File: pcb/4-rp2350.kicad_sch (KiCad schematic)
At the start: 0 parts

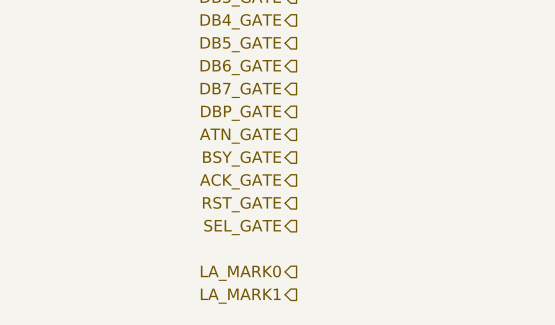
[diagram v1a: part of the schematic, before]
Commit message: Phase 3: populate SCSI sheet and channel sheets
SCSI sheet (A2): IDC50 and HD50 wired by signal name from SCSI-2
Table 2, all four RESERVED lines grounded through 0R links, the
logic-analyzer header as a pin-for-pin copy of the Digital Discovery
DIN connector, three SN74LVTH245A terminators with their DIP-switch
enable and truth table, and one cluster per line: 2 x 220R terminator
pair, ESD diode and channel sheet. Channel sheets hold the FDV301N
driver and the 74LVC1G17 receiver; 18 instances, references page x 100.

Generator: repeated sheets, sheet symbols, native tables, and
deterministic UUIDs. Nets renamed: LA -> LOGIC_ANALYZER,
TERMINATOR_EN -> TERMINATOR_EN_INVERTED_FIRMWARE.
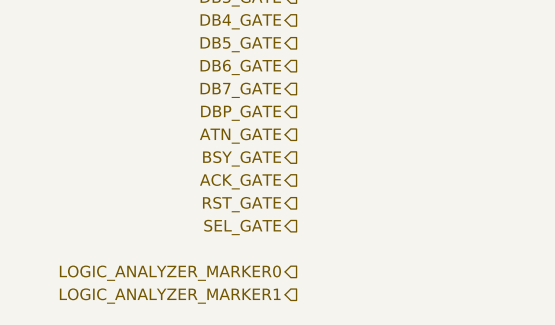
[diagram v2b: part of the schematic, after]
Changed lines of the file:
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@@
 		)
 	)
-	(hierarchical_label "LA_MARK0"
+	(hierarchical_label "LOGIC_ANALYZER_MARKER0"
 		(shape output)
 		(at 50.8 137.16 180)
@@
 		)
 	)
-	(hierarchical_label "LA_MARK1"
+	(hierarchical_label "LOGIC_ANALYZER_MARKER1"
 		(shape output)
 		(at 50.8 139.7 180)

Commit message: Phase 3: populate RP2350 sheet; FT_* nets renamed FT232H_*
RP2350 sheet (A2): RP2350B with every pin labelled by function and the
FT1248, marker and USB series resistors inline on their pins; core
regulator, per-pin decoupling (14 x 100 nF, count corrected), crystal,
QSPI flash and PSRAM in separate boxes, TC2030 debug pads and buttons,
the FT1248 rework links, and the TERMPWR sense divider on ADC6.

Generator: recursive derived-symbol flattening, small field fonts.
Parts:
- added C401, C402, C403, C404: 4.7uF 10V, Capacitor_SMD:C_0402_1005Metric, symbol Device:C
- added C405: 10uF 25V, Capacitor_SMD:C_0805_2012Metric, symbol Device:C
- added C406, C407, C408, C409, C410, C411, C412, C413, C414, C415, C416, C417, C418, C421, C422, C424: 100nF, Capacitor_SMD:C_0402_1005Metric, symbol Device:C
- added C419, C420: 15pF, Capacitor_SMD:C_0402_1005Metric, symbol Device:C
- added C423: 1uF 25V, Capacitor_SMD:C_0402_1005Metric, symbol Device:C
- added J401: TC2030-IDC, Connector:Tag-Connect_TC2030-IDC-FP_2x03_P1.27mm_Vertical, symbol Connector:TC2030
- added L401: 3.3uH, symbol Device:L
- added R401, R407, R408, R409, R410, R411, R412, R413: 33R, Resistor_SMD:R_0402_1005Metric, symbol Device:R
- added R402, R405, R406: 1k, Resistor_SMD:R_0402_1005Metric, symbol Device:R
- added R403: 3.3k, Resistor_SMD:R_0402_1005Metric, symbol Device:R
- added R404: 10k, Resistor_SMD:R_0402_1005Metric, symbol Device:R
- added R414, R415: 100R, Resistor_SMD:R_0402_1005Metric, symbol Device:R
- added R416, R417: 27R, Resistor_SMD:R_0603_1608Metric, symbol Device:R
- added R418, R419, R420, R421, R422, R423, R424, R425, R426, R427: 0R, Resistor_SMD:R_0402_1005Metric, symbol Device:R
- added R428, R429: 100k, Resistor_SMD:R_0402_1005Metric, symbol Device:R
- added SW401: BOOTSEL, symbol Switch:SW_Push
- added SW402: RUN, symbol Switch:SW_Push
- added U401: RP2350B, Package_DFN_QFN:QFN-80-1EP_10x10mm_P0.4mm_EP3.4x3.4mm, symbol MCU_RaspberryPi:RP2350B
- added U402: W25Q128JVSIQ, Package_SO:SOIC-8_5.3x5.3mm_P1.27mm, symbol Memory_Flash:W25Q128JVS
- added U403: APS6404L-3SQR-SN, Package_SO:SOIC-8_3.9x4.9mm_P1.27mm, symbol Memory_RAM:APS6404L-3SQRx-SN
- added Y401: 12MHz ABM8-272-T3, Crystal:Crystal_SMD_3225-4Pin_3.2x2.5mm, symbol Device:Crystal_GND24
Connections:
- net ACK_GATE: now also U401.37 (GPIO29)
- net ACK_RX: now also U401.9 (GPIO11)
- net ATN_GATE: now also U401.28 (GPIO27)
- net ATN_RX: now also U401.7 (GPIO9)
- net BSY_GATE: now also U401.36 (GPIO28)
- net BSY_RX: now also U401.8 (GPIO10)
- net CD_RX: now also U401.14 (GPIO15)
- net DB0_GATE: now also U401.18 (GPIO18)
- net DB0_RX: now also U401.77 (GPIO0)
- net DB1_GATE: now also U401.19 (GPIO19)
- net DB1_RX: now also U401.78 (GPIO1)
- net DB2_GATE: now also U401.20 (GPIO20)
- net DB2_RX: now also U401.79 (GPIO2)
- net DB3_GATE: now also U401.21 (GPIO21)
- net DB3_RX: now also U401.80 (GPIO3)
- net DB4_GATE: now also U401.22 (GPIO22)
- net DB4_RX: now also U401.1 (GPIO4)
- net DB5_GATE: now also U401.23 (GPIO23)
- net DB5_RX: now also U401.2 (GPIO5)
- net DB6_GATE: now also U401.25 (GPIO24)
- net DB6_RX: now also U401.3 (GPIO6)
- net DB7_GATE: now also U401.26 (GPIO25)
- net DB7_RX: now also U401.4 (GPIO7)
- net DBP_GATE: now also U401.27 (GPIO26)
- net DBP_RX: now also U401.6 (GPIO8)
- net I2C_SCL: now also R420.2
- net I2C_SDA: now also R418.2
- net IO_RX: now also U401.17 (GPIO17)
- net LOGIC_ANALYZER_MARKER0: now also R414.1
- net LOGIC_ANALYZER_MARKER1: now also R415.1
- net MSG_RX: now also U401.12 (GPIO13)
- net REQ_RX: now also U401.16 (GPIO16)
- net RST_GATE: now also U401.38 (GPIO30)
- net RST_RX: now also U401.11 (GPIO12)
- net SD_CLK: now also R422.2
- net SD_CMD: now also R424.2
- net SD_D0: now also R426.2
- net SEL_GATE: now also U401.39 (GPIO31)
- net SEL_RX: now also U401.13 (GPIO14)
- net USB_RP_D+: now also R416.1
- net USB_RP_D-: now also R417.1
- new net: R407.1, U401.40 (GPIO32)
- new net: R408.1, U401.42 (GPIO33)
- new net: R409.1, U401.43 (GPIO34)
- new net: R410.1, U401.44 (GPIO35)
- new net: R411.2, U401.52 (GPIO41/ADC1)
- new net: R412.2, U401.53 (GPIO42/ADC2)
- new net: R413.2, U401.54 (GPIO43/ADC3)
- new net: R414.2, U401.55 (GPIO44/ADC4)
- new net: R415.2, U401.56 (GPIO45/ADC5)
- new net: R417.2, U401.66 (USB_DM)
- new net: R416.2, U401.67 (USB_DP)
- new net: R405.2, SW401.1
- new net: C420.1, R402.1, Y401.3
- new net: R406.2, SW402.1
- new net +3V3: C402.1, C405.1, C406.1, C407.1, C408.1, C409.1, C410.1, C411.1, C412.1, C413.1, C417.1, C418.1, C421.1, C422.1, C423.1, J401.1, R401.1, R403.1, R404.1, U401.15 (IOVDD), U401.24 (IOVDD), U401.29 (IOVDD), U401.41 (IOVDD), U401.5 (IOVDD), U401.50 (IOVDD), U401.59 (ADC_AVDD), U401.60 (IOVDD), U401.64 (VREG_VIN), U401.68 (USB_OTP_VDD), U401.69 (QSPI_IOVDD), U401.76 (IOVDD), U402.8 (VCC), U403.8 (VDD)
- new net DVDD_1V1: C403.1, C404.1, C414.1, C415.1, C416.1, L401.2, U401.10 (DVDD), U401.32 (DVDD), U401.51 (DVDD), U401.65 (VREG_FB)
- new net FT232H_D4: R419.2
- new net FT232H_D5: R421.2
- new net FT232H_D6: R423.2
- new net FT232H_D7: R425.2
- new net FT232H_MIOSIO0: R407.2
- new net FT232H_MIOSIO1: R408.2
- new net FT232H_MIOSIO2: R409.2
- new net FT232H_MIOSIO3: R410.2
- new net FT232H_MISO: R413.1
- new net FT232H_SCLK: R411.1
- new net FT232H_SS_N: R412.1
- new net FT232H_WR_N: R427.2
- new net GND: C401.2, C402.2, C403.2, C404.2, C405.2, C406.2, C407.2, C408.2, C409.2, C410.2, C411.2, C412.2, C413.2, C414.2, C415.2, C416.2, C417.2, C418.2, C419.2, C420.2, C421.2, C422.2, C423.2, C424.2, J401.5, R429.2, SW401.2, SW402.2, U401.62 (VREG_PGND), U401.81 (GND), U402.4 (GND), U403.4 (VSS), Y401.2 (G), Y401.4 (G)
- new net GPIO36: R418.1, R419.1, U401.45 (GPIO36)
- new net GPIO37: R420.1, R421.1, U401.46 (GPIO37)
- new net GPIO38: R422.1, R423.1, U401.47 (GPIO38)
- new net GPIO39: R424.1, R425.1, U401.48 (GPIO39)
- new net GPIO40: R426.1, R427.1, U401.49 (GPIO40/ADC0)
- new net PSRAM_CE_INVERTED: R403.2, U401.58 (GPIO47/ADC7), U403.1 (~{CE})
- new net QSPI_SCLK: U401.71 (QSPI_SCLK), U402.6 (CLK), U403.6 (SCLK)
- new net QSPI_SD0: U401.72 (QSPI_SD0), U402.5 (DI/IO_{0}), U403.5 (SI/SIO0)
- new net QSPI_SD1: U401.74 (QSPI_SD1), U402.2 (DO/IO_{1}), U403.2 (SO/SIO1)
- new net QSPI_SD2: U401.73 (QSPI_SD2), U402.3 (~{WP}/IO_{2}), U403.3 (SIO2)
- new net QSPI_SD3: U401.70 (QSPI_SD3), U402.7 (~{HOLD}/~{RESET}/IO_{3}), U403.7 (SIO3)
- new net QSPI_SS_INVERTED: R404.2, R405.1, U401.75 (~{QSPI_SS}), U402.1 (~{CS})
- new net RUN: J401.3, R406.1, U401.35 (RUN)
- new net SWCLK: J401.4, U401.33 (SWCLK)
- new net SWDIO: J401.2, U401.34 (SWDIO)
- new net TERMPWR: R428.1
- new net TERMPWR_SENSE: C424.1, R428.2, R429.1, U401.57 (GPIO46/ADC6)
- new net VREG_AVDD: C401.1, R401.2, U401.61 (VREG_AVDD)
- new net VREG_LX: L401.1, U401.63 (VREG_LX)
- new net XIN: C419.1, U401.30 (XIN), Y401.1
- new net XOUT: R402.2, U401.31 (XOUT)
- no-connect marks 0 -> 1
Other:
- note added: "0.5 x TERMPWR on GPIO 46: 0-5.6 V -> 0-2.8 V. Draws 26 uA from TERMPWR."
- note added: "ABM8-272-T3 (CL 10 pF, ESR <= 50 R): 2 x 15 pF (7.5 pF + ~3 pF stray), 1k series on XOUT stops overdrive."
- note added: "ADC_AVDD 59"
- note added: "APS6404L-3SQR-SN, 8 MB, on CS1 = GPIO 47: the stall buffer between SCSI and the host."
- note added: "BOOTSEL pulls QSPI_SS low through 1k at reset; RUN has no pull-up (the guide fits none; the RP2350 pulls RUN up internally)."
- note added: "C402 CIN, C403 COUT, C404 2nd DVDD (all 4.7 uF 0402; fallback 0603 C19666 for CIN if DC bias bites)."
- note added: "Core regulator (on-chip, 1.1 V)"
- note added: "Crystal (12 MHz)"
- note added: "DVDD 10"
- note added: "DVDD 32"
- note added: "DVDD 51"
- note added: "Debug and buttons"
- note added: "Decoupling (100 nF per supply pin, at the pin)"
- note added: "FT1248 rework links"
- note added: "Firmware keeps GPIO 46's digital input buffer off (analog use)."
- note added: "Fitted 0R: GPIO 36-40 -> I2C / microSD (normal). Unfitted 0R: the same GPIO -> FT232H pins 17-20, 27. Moving the links trades I2C + microSD for 8-bit FT1248 (36-39) or 245-FIFO mode (36-40)."
- note added: "Guide 2.1 / datasheet 6.3.8. Layout: inductor orientation per Fig. 23, VREG_PGND and CIN straight to the exposed pad, and a ground cut-out under VREG_LX on layer 2 (Fig. 24)."
- note added: "I2C0 SCL (rework: FT232H_D5)"
- note added: "I2C0 SDA (rework: FT232H_D4)"
- note added: "IOVDD 15"
- note added: "IOVDD 24"
- note added: "IOVDD 29"
- note added: "IOVDD 41"
- note added: "IOVDD 5"
- note added: "IOVDD 50"
- note added: "IOVDD 60"
- note added: "IOVDD 76"
- note added: "PSRAM"
- note added: "PWR_FLAGs: DVDD_1V1 is fed through L401 and VREG_AVDD through R401, which ERC sees as passive parts."
- note added: "Pin map: blocks/5-rp2350-pinout.md. GPIO 0-17 = receiver outputs (PIO0 in, read inverted), GPIO 18-31 = driver gates (1 = asserted). The only ground is the exposed pad (pin 81). Series resistors sit at the pins: 33R on the 7 FT1248 nets (damps ringing at 25 MHz, limits contention), 100R on the logic-analyzer markers, 27R 0603 on native USB (close to the chip)."
- note added: "Polarity dot per datasheet Fig. 23; check JLC's placement preview."
- note added: "QSPI flash"
- note added: "R403 3.3k: the RP2350 pulls GPIO 47 low at reset (36k min); 10k gave 2.58 V, under the PSRAM's VIH (VDD - 0.4 V). 3.3k gives 3.02 V."
- note added: "R404 DNP: this flash doesn't need a CS pull-up (guide R1)."
- note added: "RP2350B"
- note added: "TERMPWR sense (ADC6)"
- note added: "Tag-Connect TC2030-IDC pads (no part on the BOM) for the J-Link EDU via an ARM20-CTX adapter. BOOTSEL + reset = USB bootloader; normally the host enters BOOTSEL in software."
- note added: "Top pins: USB_OTP_VDD, ADC_AVDD, QSPI_IOVDD, IOVDD (x8) and VREG_VIN share +3V3; VREG_FB and DVDD (x3) are the 1.1 V core rail (DVDD_1V1), made by the on-chip regulator. Each supply pin gets its own 100 nF (Decoupling box)."
- note added: "USB_OTP 68+ QSPI 69"
- note added: "W25Q128JVSIQ, 16 MB, on the dedicated chip select (QSPI_SS). Boot + firmware."
- note added: "microSD CLK (rework: FT232H_D6)"
- note added: "microSD CMD (rework: FT232H_D7)"
- note added: "microSD D0 (rework: FT232H_WR_N)"
- note removed: "RP2350B and support (blocks/3-mcu-support.md, pin map blocks/5-rp2350-pinout.md) RP2350B + core regulator (3.3 µH, 4 × 4.7 µF, 33 Ω), decoupling, 12 MHz crystal, W25Q128 flash, APS6404L PSRAM (CS1 = GPIO 47, 3.3 k up), TC2030 SWD, BOOTSEL/RUN, 27 Ω USB series R, 33 Ω FT1248 series R, FT1248 rework 0 Ω links (GPIO 36-40), LA marker 100 Ω, TERMPWR ADC divider 100 k/100 k + 100 nF on GPIO 46."

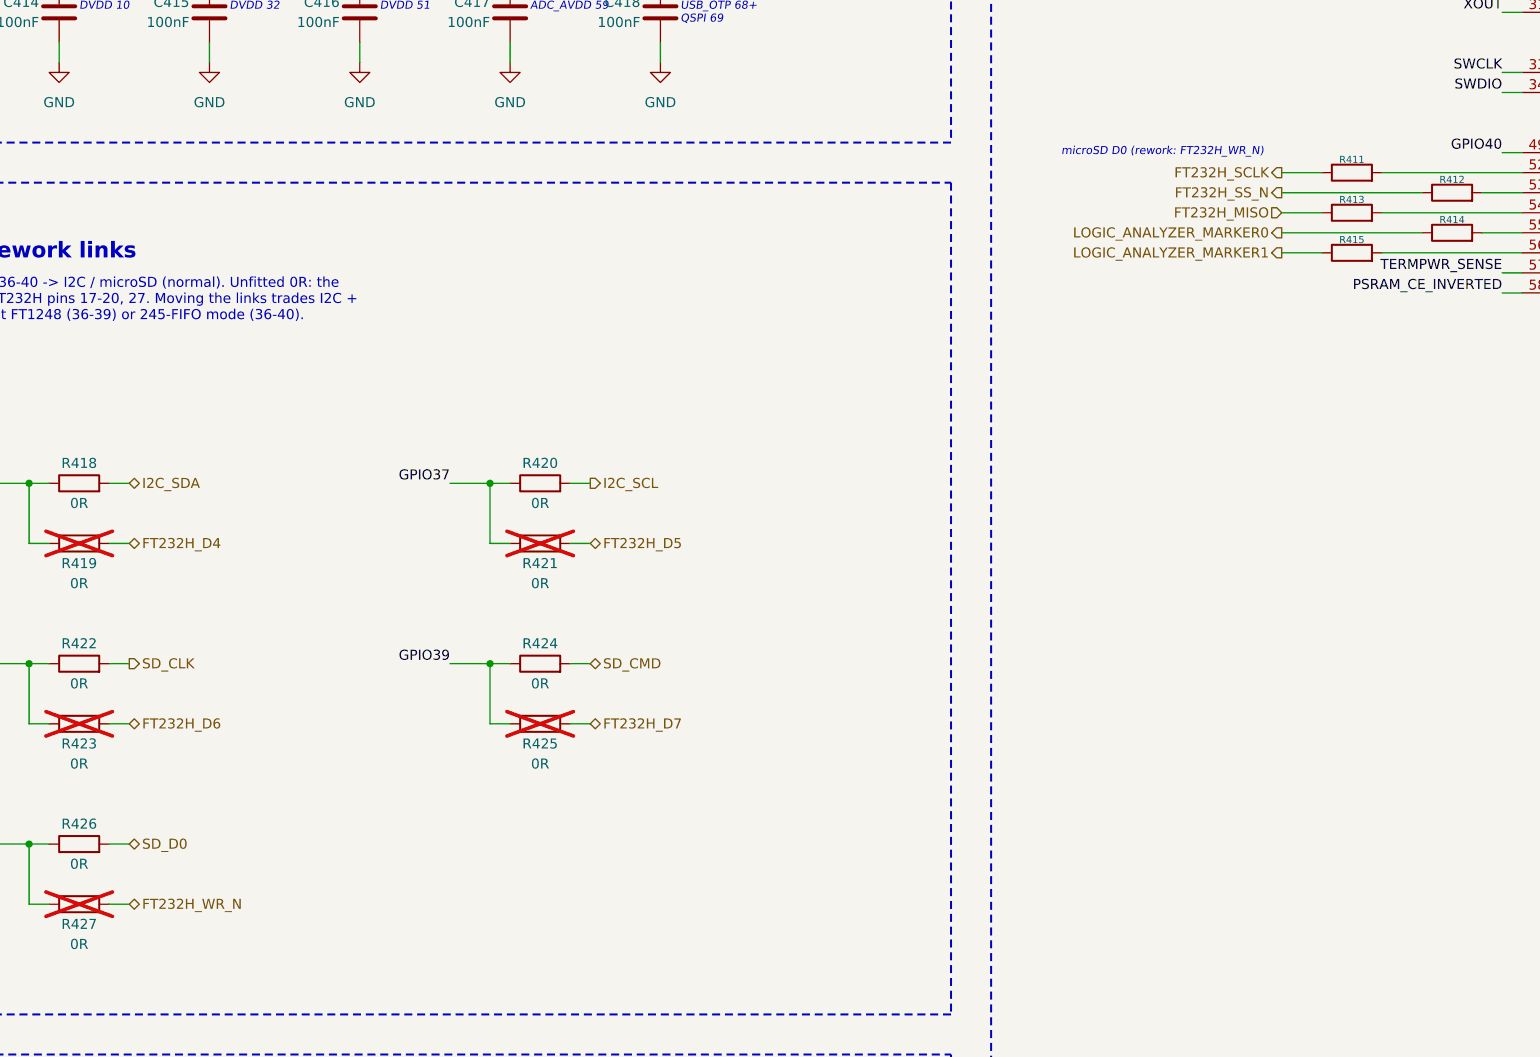
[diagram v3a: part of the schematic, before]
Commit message: Phase 3: populate FT232H sheet; FT232H_WR_N -> FT232H_WRITE_INVERTED
FT232HL per DS Fig. 6.2 (VCCD makes FT232H_3V3), ferrite-fed VPHY/VPLL,
93LC56B config EEPROM, crystal, REF, RESET RC and FIFO-fallback pull-ups.
Project FT232H symbol retypes EECS/EECLK as outputs (and VCCD as
power_out); upstream fix recorded as a follow-up (NOTES open question 14).
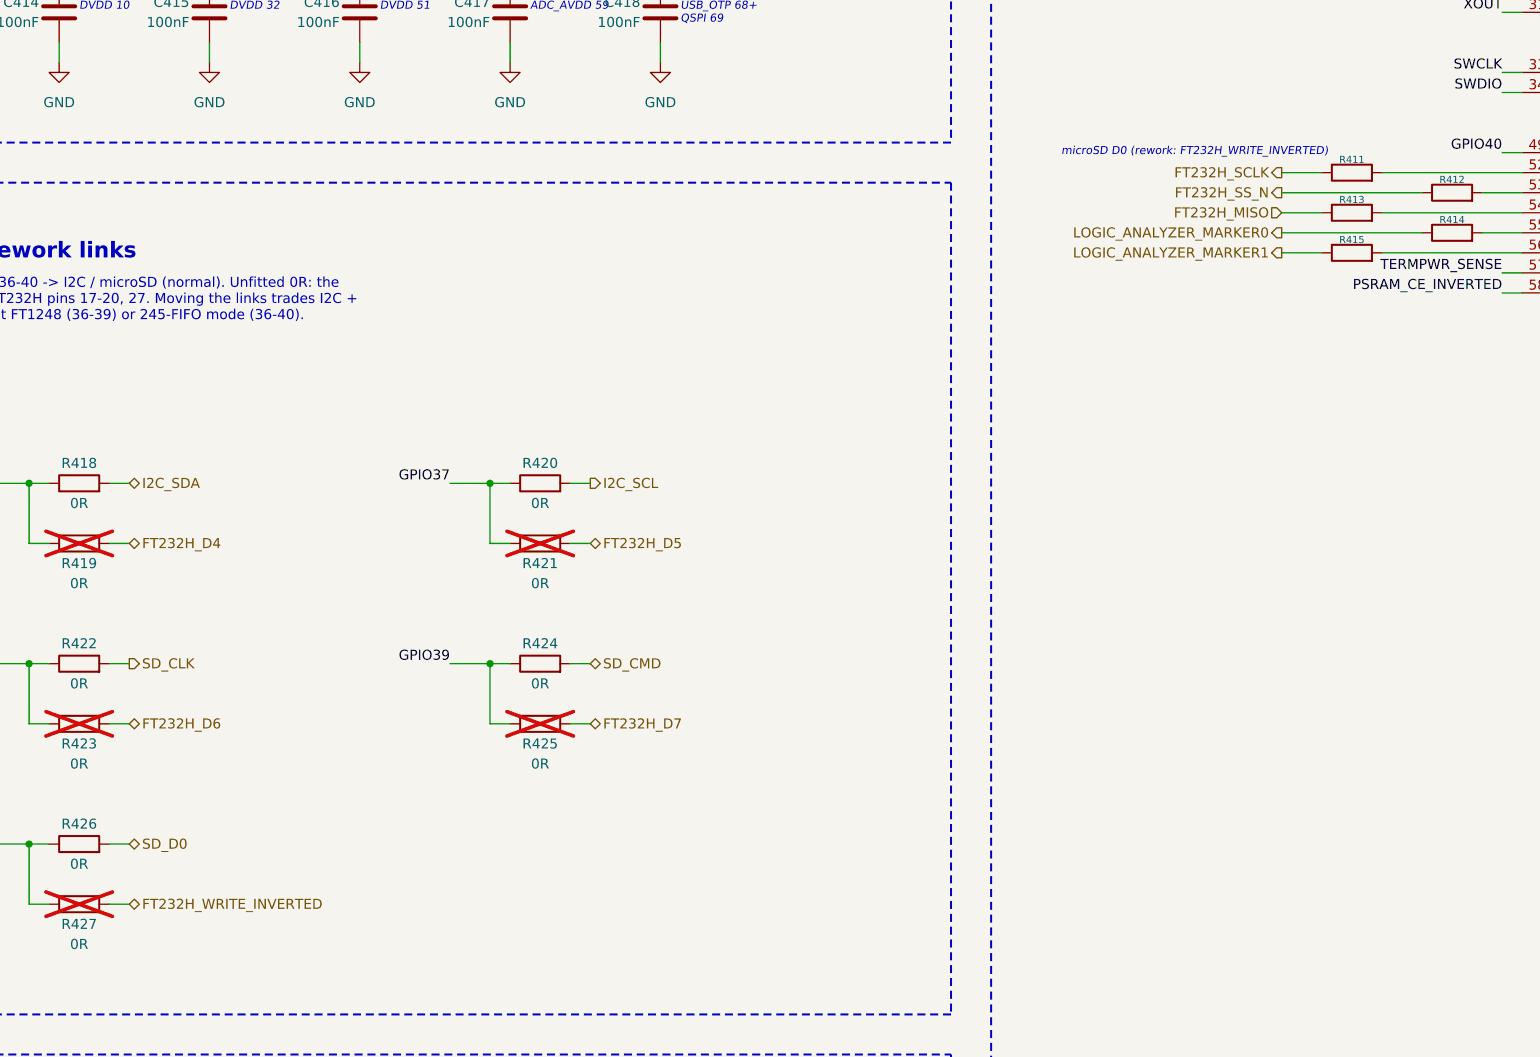
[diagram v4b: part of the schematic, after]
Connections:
- net FT232H_WR_N renamed FT232H_WRITE_INVERTED
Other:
- note added: "microSD D0 (rework: FT232H_WRITE_INVERTED)"
- note removed: "microSD D0 (rework: FT232H_WR_N)"
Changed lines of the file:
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@@
 	(text "microSD CLK (rework: FT232H_D6)" (exclude_from_sim no) (at 290.83 206.375 0) (effects (font (size 1.016 1.016) (italic yes)) (justify left top)))
 	(text "microSD CMD (rework: FT232H_D7)" (exclude_from_sim no) (at 290.83 208.915 0) (effects (font (size 1.016 1.016) (italic yes)) (justify left top)))
-	(text "microSD D0 (rework: FT232H_WR_N)" (exclude_from_sim no) (at 168.91 191.135 0) (effects (font (size 1.016 1.016) (italic yes)) (justify left top)))
+	(text "microSD D0 (rework: FT232H_WRITE_INVERTED)" (exclude_from_sim no) (at 168.91 191.135 0) (effects (font (size 1.016 1.016) (italic yes)) (justify left top)))
 	(wire (pts (xy 240.03 102.87) (xy 240.03 97.79)) (stroke (width 0) (type default)))
 	(wire (pts (xy 242.57 102.87) (xy 242.57 97.79)) (stroke (width 0) (type default)))
@@
 	)
 	(wire (pts (xy 48.26 287.02) (xy 50.8 287.02)) (stroke (width 0) (type default)))
-	(hierarchical_label "FT232H_WR_N" (shape bidirectional) (at 50.8 287.02 0) (effects (font (size 1.27 1.27)) (justify left)))
+	(hierarchical_label "FT232H_WRITE_INVERTED" (shape bidirectional) (at 50.8 287.02 0) (effects (font (size 1.27 1.27)) (justify left)))
 	(wire (pts (xy 38.1 287.02) (xy 40.64 287.02)) (stroke (width 0) (type default)))
 	(rectangle (start 12.7 306.07) (end 154.94 406.4) (stroke (width 0.254) (type dash)) (fill (type none)))

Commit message: Phase 3: footprint audit fixes and project footprint library
- New project footprint library pcb/scsi-adapter.pretty, generated by
  pcb/_gen/footprints.py from datasheet land patterns: TI RPW0010A (U101/U201),
  Kangnex WJ500V (J101), TE AMPLIMITE .050 HD50 (J302), SHOU HAN TF PUSH
  microSD (J501), Abracon AOTA-B201610 polarized inductor (L401), SHOU HAN
  2-pos DIP (SW301). fp-lib-table added.
- J303 LA header: 2x17 box header C20920, pins 33/34 NC (34-way ribbon to a
  future 2x16 adapter board).
- J302 HD50: TE 5787082-5 squeeze-latch receptacle; shielded symbol, shell to
  GND via R343 0R. TE STEP model git-ignored (pcb/scsi-adapter.3dshapes/).
- D101/D204/D605: D_SMF -> D_SOD-123F (parts are SOD-123FL).
- L401 pins swapped so pad 1 = polarity dot = DVDD_1V1 (RP2350 Fig. 23).
- SW401/SW402: Hroparts K2-1102DP C110153 on SW_PUSH_6mm.
- NOTES, decisions, sources updated; J601 pad question closed; RP2350B
  minimal-design layout copy planned (open question 17).
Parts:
- L401: footprint (none) -> scsi-adapter:L_Abracon_AOTA-B201610_2.0x1.6mm_Polarized
- SW401, SW402: footprint (none) -> Button_Switch_THT:SW_PUSH_6mm; LCSC (none) -> C110153
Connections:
- net DVDD_1V1: now also L401.1; no longer L401.2
- net VREG_LX: now also L401.2; no longer L401.1
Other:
- note added: "Pin 1 = the part's dot = DVDD_1V1 (datasheet Fig. 23, Pico 2 layout). Check JLC's placement preview."
- note removed: "Polarity dot per datasheet Fig. 23; check JLC's placement preview."
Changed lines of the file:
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@@
 		(property "Reference" "L401" (at 60.96 46.99 90) (effects (font (size 1.27 1.27))))
 		(property "Value" "3.3uH" (at 60.96 54.61 90) (effects (font (size 1.27 1.27))))
-		(property "Footprint" "" (at 60.96 50.8 0) (effects (font (size 1.27 1.27)) (hide yes)))
+		(property "Footprint" "scsi-adapter:L_Abracon_AOTA-B201610_2.0x1.6mm_Polarized" (at 60.96 50.8 0) (effects (font (size 1.27 1.27)) (hide yes)))
 		(property "Datasheet" "" (at 60.96 50.8 0) (effects (font (size 1.27 1.27)) (hide yes)))
-		(property "Description" "Abracon AOTA-B201610S3R3-101-T, polarity-marked (datasheet requires it). 2016 footprint with polarity mark to do." (at 60.96 50.8 0) (effects (font (size 1.27 1.27)) (hide yes)))
+		(property "Description" "Abracon AOTA-B201610S3R3-101-T, polarity-marked: pad 1 = dot = DVDD (RP2350 Fig. 23)" (at 60.96 50.8 0) (effects (font (size 1.27 1.27)) (hide yes)))
 		(property "LCSC" "C42411119" (at 60.96 50.8 0) (effects (font (size 1.27 1.27)) (hide yes)))
 		(property "Fit" "JLC" (at 60.96 50.8 0) (effects (font (size 1.27 1.27)) (hide yes)))
@@
 	)
 	(wire (pts (xy 57.15 50.8) (xy 54.61 50.8)) (stroke (width 0) (type default)))
-	(label "VREG_LX" (at 54.61 50.8 180) (effects (font (size 1.27 1.27)) (justify right bottom)))
+	(label "DVDD_1V1" (at 54.61 50.8 180) (effects (font (size 1.27 1.27)) (justify right bottom)))
 	(wire (pts (xy 64.77 50.8) (xy 67.31 50.8)) (stroke (width 0) (type default)))
-	(label "DVDD_1V1" (at 67.31 50.8 0) (effects (font (size 1.27 1.27)) (justify left bottom)))
-	(text "Polarity dot per datasheet Fig. 23;\ncheck JLC's placement preview." (exclude_from_sim no) (at 43.18 58.42 0) (effects (font (size 1.016 1.016) (italic yes)) (justify left top)))
+	(label "VREG_LX" (at 67.31 50.8 0) (effects (font (size 1.27 1.27)) (justify left bottom)))
+	(text "Pin 1 = the part's dot = DVDD_1V1 (datasheet Fig. 23,\nPico 2 layout). Check JLC's placement preview." (exclude_from_sim no) (at 43.18 58.42 0) (effects (font (size 1.016 1.016) (italic yes)) (justify left top)))
 	(symbol (lib_id "power:PWR_FLAG") (at 81.28 38.1 0) (unit 1) (exclude_from_sim no) (in_bom no) (on_board no) (dnp no)
 		(property "Reference" "#FLG401" (at 81.28 33.02 0) (effects (font (size 1.27 1.27)) (justify left) (hide yes)))
@@
 		(property "Reference" "SW401" (at 462.28 232.41 270) (effects (font (size 1.27 1.27)) (justify right)))
 		(property "Value" "BOOTSEL" (at 462.28 234.95 270) (effects (font (size 1.27 1.27)) (justify right)))
-		(property "Footprint" "" (at 459.74 233.68 0) (effects (font (size 1.27 1.27)) (hide yes)))
+		(property "Footprint" "Button_Switch_THT:SW_PUSH_6mm" (at 459.74 233.68 0) (effects (font (size 1.27 1.27)) (hide yes)))
 		(property "Datasheet" "" (at 459.74 233.68 0) (effects (font (size 1.27 1.27)) (hide yes)))
-		(property "Description" "Owner's through-hole tact switch; footprint to do once the part is checked" (at 459.74 233.68 0) (effects (font (size 1.27 1.27)) (hide yes)))
-		(property "LCSC" "" (at 459.74 233.68 0) (effects (font (size 1.27 1.27)) (hide yes)))
+		(property "Description" "Hroparts K2-1102DP-C4SW-04 6x6x5 THT tact (LCSC, hand-fit); alt TE 1825910-6. Route to diagonal legs" (at 459.74 233.68 0) (effects (font (size 1.27 1.27)) (hide yes)))
+		(property "LCSC" "C110153" (at 459.74 233.68 0) (effects (font (size 1.27 1.27)) (hide yes)))
 		(property "Fit" "Hand" (at 459.74 233.68 0) (effects (font (size 1.27 1.27)) (hide yes)))
 		(pin "1")
@@
 		(property "Reference" "SW402" (at 508 232.41 270) (effects (font (size 1.27 1.27)) (justify right)))
 		(property "Value" "RUN" (at 508 234.95 270) (effects (font (size 1.27 1.27)) (justify right)))
-		(property "Footprint" "" (at 505.46 233.68 0) (effects (font (size 1.27 1.27)) (hide yes)))
+		(property "Footprint" "Button_Switch_THT:SW_PUSH_6mm" (at 505.46 233.68 0) (effects (font (size 1.27 1.27)) (hide yes)))
 		(property "Datasheet" "" (at 505.46 233.68 0) (effects (font (size 1.27 1.27)) (hide yes)))
-		(property "Description" "Owner's through-hole tact switch; footprint to do once the part is checked" (at 505.46 233.68 0) (effects (font (size 1.27 1.27)) (hide yes)))
-		(property "LCSC" "" (at 505.46 233.68 0) (effects (font (size 1.27 1.27)) (hide yes)))
+		(property "Description" "Hroparts K2-1102DP-C4SW-04 6x6x5 THT tact (LCSC, hand-fit); alt TE 1825910-6. Route to diagonal legs" (at 505.46 233.68 0) (effects (font (size 1.27 1.27)) (hide yes)))
+		(property "LCSC" "C110153" (at 505.46 233.68 0) (effects (font (size 1.27 1.27)) (hide yes)))
 		(property "Fit" "Hand" (at 505.46 233.68 0) (effects (font (size 1.27 1.27)) (hide yes)))
 		(pin "1")
